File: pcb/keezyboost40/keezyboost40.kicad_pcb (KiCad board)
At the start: 2 copper layers, 217.6 x 68.1 mm, 92 parts, among them SW1 SW_SPST, SW10 SW_SPST, SW11 SW_SPST, SW12 SW_SPST, SW13 SW_SPST, SW14 SW_SPST, SW15 SW_SPST, SW16 SW_SPST, SW17 SW_SPST, SW18 SW_SPST, SW19 SW_SPST, SW2 SW_SPST, SW20 SW_SPST, SW21 SW_SPST, SW22 SW_SPST, SW23 SW_SPST, SW24 SW_SPST, SW25 SW_SPST, SW26 SW_SPST, SW27 SW_SPST, SW28 SW_SPST, SW29 SW_SPST, SW3 SW_SPST, SW30 SW_SPST, SW31 SW_SPST, SW32 SW_SPST, SW33 SW_SPST, SW34 SW_SPST, SW35 SW_SPST, SW36 SW_SPST, SW37 SW_SPST, SW38 SW_SPST, SW39 SW_SPST, SW4 SW_SPST, SW40 SW_SPST, SW5 SW_SPST, SW6 SW_SPST, SW7 SW_SPST, SW8 SW_SPST, SW9 SW_SPST, U1 Pico, U2 ST7735_1.8inch

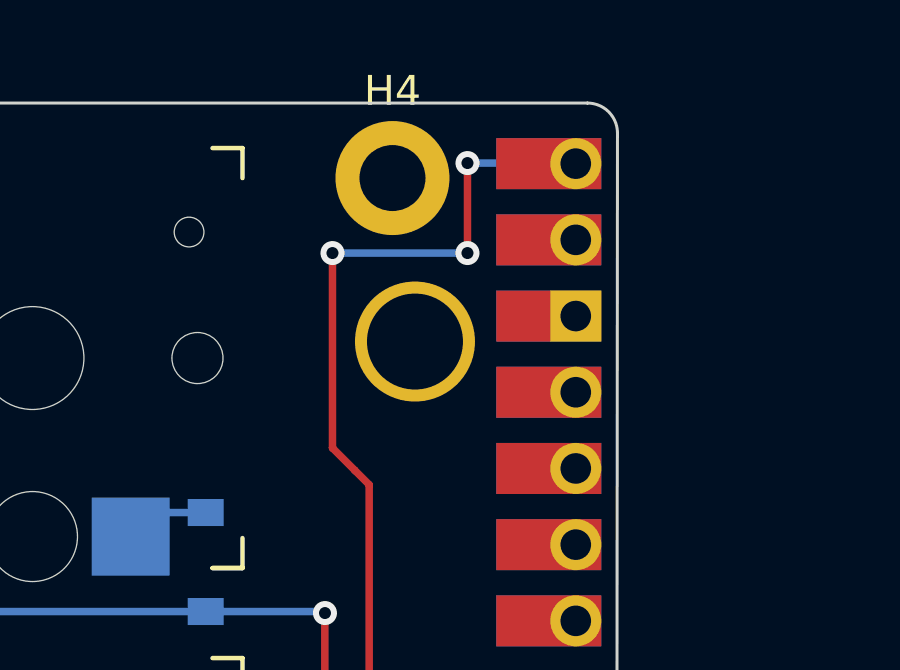
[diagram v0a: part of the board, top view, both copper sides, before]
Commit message: make lcd use 3.3v over 5v
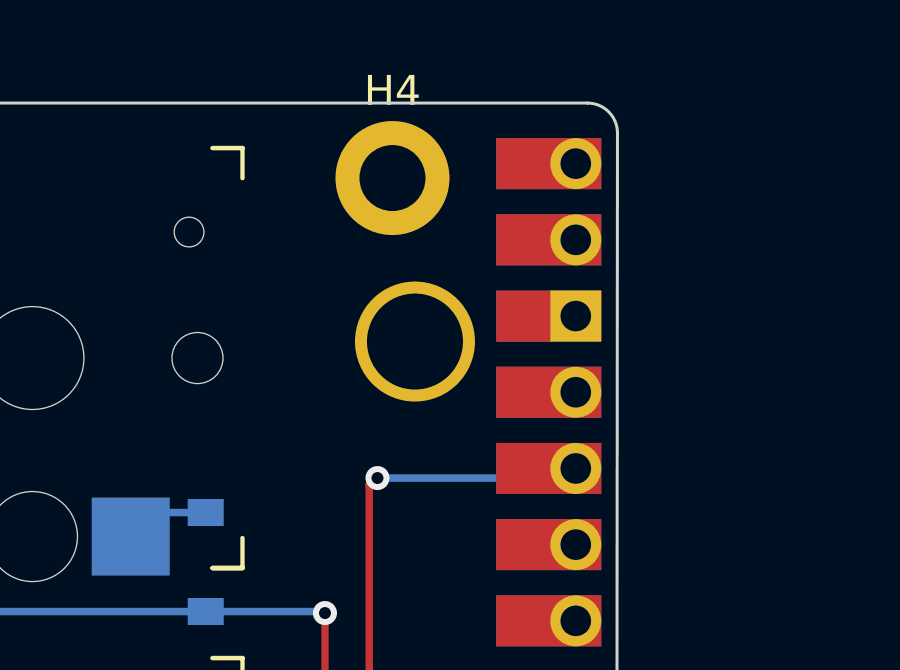
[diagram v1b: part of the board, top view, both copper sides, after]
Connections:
- U1 pad 36: unconnected-(U1-Pad36) -> vcc
- U1 pad 40: vcc -> unconnected-(U1-Pad40)
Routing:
- net vcc: track 73.1 -> 60.8 mm, vias 5 -> 3
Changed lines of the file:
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@@
   (net 68 "sck")
   (net 69 "sda")
-  (net 70 "unconnected-(U1-Pad36)")
+  (net 70 "unconnected-(U1-Pad40)")
   (net 71 "unconnected-(U1-Pad28)")
   (net 72 "unconnected-(U1-Pad30)")
@@
       (net 75 "unconnected-(U1-Pad35)") (pinfunction "ADC_VREF") (pintype "power_in+no_connect"))
     (pad "36" smd rect locked (at 8.89 13.97) (size 3.5 1.7) (drill (offset -0.9 0)) (layers "F.Cu" "F.Mask")
-      (net 70 "unconnected-(U1-Pad36)") (pinfunction "3V3") (pintype "power_in+no_connect"))
+      (net 78 "vcc") (pinfunction "3V3") (pintype "power_in"))
     (pad "36" thru_hole oval locked (at 8.89 13.97 180) (size 1.7 1.7) (drill 1.02) (layers *.Cu *.Mask)
-      (net 70 "unconnected-(U1-Pad36)") (pinfunction "3V3") (pintype "power_in+no_connect"))
+      (net 78 "vcc") (pinfunction "3V3") (pintype "power_in"))
     (pad "36" smd rect locked (at 8.89 13.97 180) (size 3.5 1.7) (drill (offset 0.9 0)) (layers "B.Cu" "B.Mask")
-      (net 70 "unconnected-(U1-Pad36)") (pinfunction "3V3") (pintype "power_in+no_connect"))
+      (net 78 "vcc") (pinfunction "3V3") (pintype "power_in"))
     (pad "37" smd rect locked (at 8.89 16.51) (size 3.5 1.7) (drill (offset -0.9 0)) (layers "F.Cu" "F.Mask")
       (net 76 "unconnected-(U1-Pad37)") (pinfunction "3V3_EN") (pintype "input+no_connect"))
@@
       (net 77 "unconnected-(U1-Pad39)") (pinfunction "VSYS") (pintype "power_in+no_connect"))
     (pad "40" smd rect locked (at 8.89 24.13 180) (size 3.5 1.7) (drill (offset 0.9 0)) (layers "B.Cu" "B.Mask")
-      (net 78 "vcc") (pinfunction "VBUS") (pintype "power_in"))
+      (net 70 "unconnected-(U1-Pad40)") (pinfunction "VBUS") (pintype "power_in+no_connect"))
     (pad "40" thru_hole oval locked (at 8.89 24.13 180) (size 1.7 1.7) (drill 1.02) (layers *.Cu *.Mask)
-      (net 78 "vcc") (pinfunction "VBUS") (pintype "power_in"))
+      (net 70 "unconnected-(U1-Pad40)") (pinfunction "VBUS") (pintype "power_in+no_connect"))
     (pad "40" smd rect locked (at 8.89 24.13) (size 3.5 1.7) (drill (offset -0.9 0)) (layers "F.Cu" "F.Mask")
-      (net 78 "vcc") (pinfunction "VBUS") (pintype "power_in"))
+      (net 70 "unconnected-(U1-Pad40)") (pinfunction "VBUS") (pintype "power_in+no_connect"))
     (group "" (id 2eefb77a-c30b-42f2-a0dd-3b92e0293566)
       (members
@@
   (segment (start 101.862256 75.775489) (end 124.724511 75.775489) (width 0.25) (layer "B.Cu") (net 69))
   (segment (start 101.488084 76.149661) (end 101.862256 75.775489) (width 0.25) (layer "B.Cu") (net 69))
+  (segment (start 112.09 14.5) (end 112.11 14.52) (width 0.25) (layer "B.Cu") (net 70))
+  (segment (start 105.224511 25.224511) (end 105.449022 25) (width 0.25) (layer "F.Cu") (net 78))
   (segment (start 105.224511 68.322562) (end 105.5 68.598051) (width 0.25) (layer "F.Cu") (net 78))
   (segment (start 111 68.75) (end 111 71.84) (width 0.25) (layer "F.Cu") (net 78))
   (segment (start 111 71.84) (end 112.11 72.95) (width 0.25) (layer "F.Cu") (net 78))
   (segment (start 105.224511 25.224511) (end 105.224511 68.322562) (width 0.25) (layer "F.Cu") (net 78))
-  (segment (start 104.75 24.75) (end 104 24) (width 0.25) (layer "F.Cu") (net 78))
-  (segment (start 108.5 17.5) (end 108.5 14.5) (width 0.25) (layer "F.Cu") (net 78))
-  (segment (start 104.75 24.75) (end 105.224511 25.224511) (width 0.25) (layer "F.Cu") (net 78))
-  (segment (start 104 24) (end 104 17.5) (width 0.25) (layer "F.Cu") (net 78))
-  (via (at 104 17.5) (size 0.8) (drill 0.4) (layers "F.Cu" "B.Cu") (net 78))
-  (via (at 108.5 14.5) (size 0.8) (drill 0.4) (layers "F.Cu" "B.Cu") (net 78))
-  (via (at 108.5 17.5) (size 0.8) (drill 0.4) (layers "F.Cu" "B.Cu") (net 78))
+  (segment (start 105.449022 25) (end 105.5 25) (width 0.25) (layer "F.Cu") (net 78))
+  (via (at 105.5 25) (size 0.8) (drill 0.4) (layers "F.Cu" "B.Cu") (net 78))
   (via (at 111 68.75) (size 0.8) (drill 0.4) (layers "F.Cu" "B.Cu") (net 78))
   (via (at 105.5 68.598051) (size 0.8) (drill 0.4) (layers "F.Cu" "B.Cu") (net 78))
   (segment (start 110.848051 68.598051) (end 111 68.75) (width 0.25) (layer "B.Cu") (net 78))
-  (segment (start 108.5 14.5) (end 112.09 14.5) (width 0.25) (layer "B.Cu") (net 78))
-  (segment (start 104 17.5) (end 108.5 17.5) (width 0.25) (layer "B.Cu") (net 78))
+  (segment (start 105.5 25) (end 111.79 25) (width 0.25) (layer "B.Cu") (net 78))
+  (segment (start 111.79 25) (end 112.11 24.68) (width 0.25) (layer "B.Cu") (net 78))
   (segment (start 105.5 68.598051) (end 110.848051 68.598051) (width 0.25) (layer "B.Cu") (net 78))
-  (segment (start 112.09 14.5) (end 112.11 14.52) (width 0.25) (layer "B.Cu") (net 78))
   (group "" (id 7b4c85be-e685-4876-acb4-59efa78bd468)
     (members

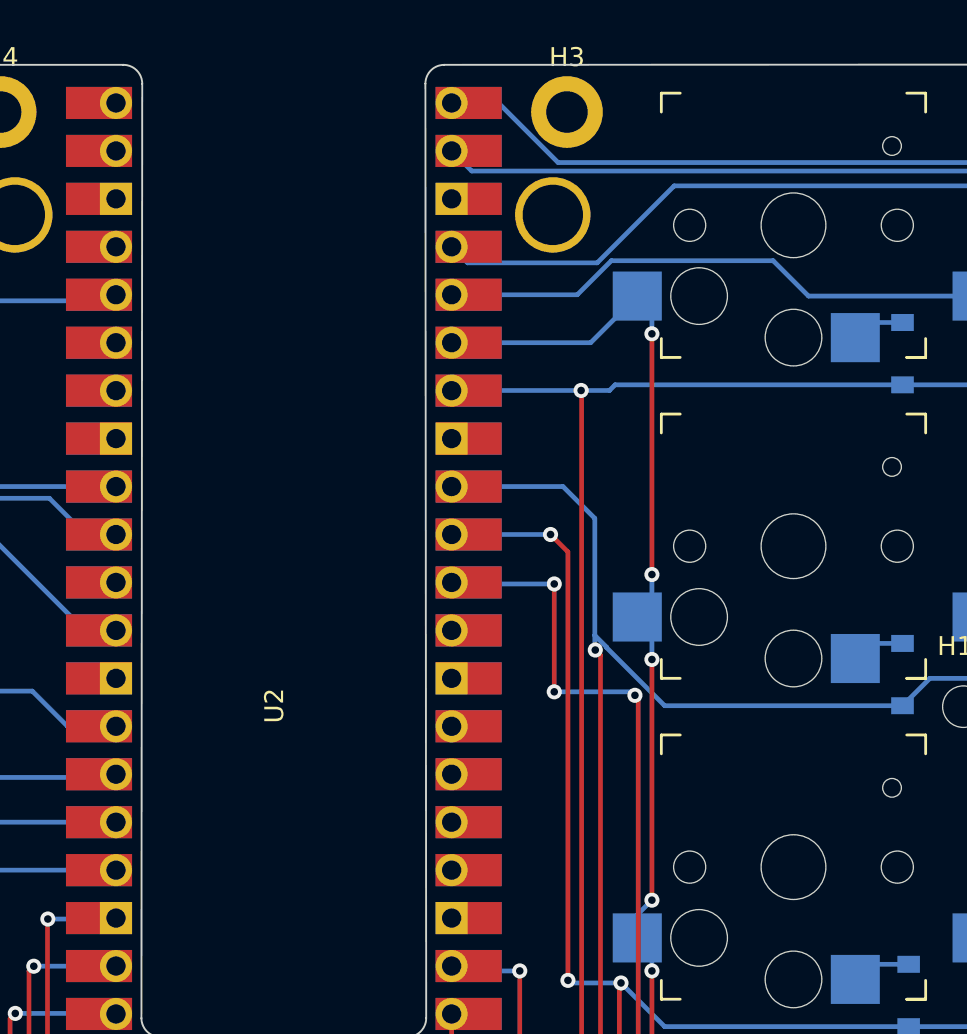
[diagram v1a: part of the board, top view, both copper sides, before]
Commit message: add reset button
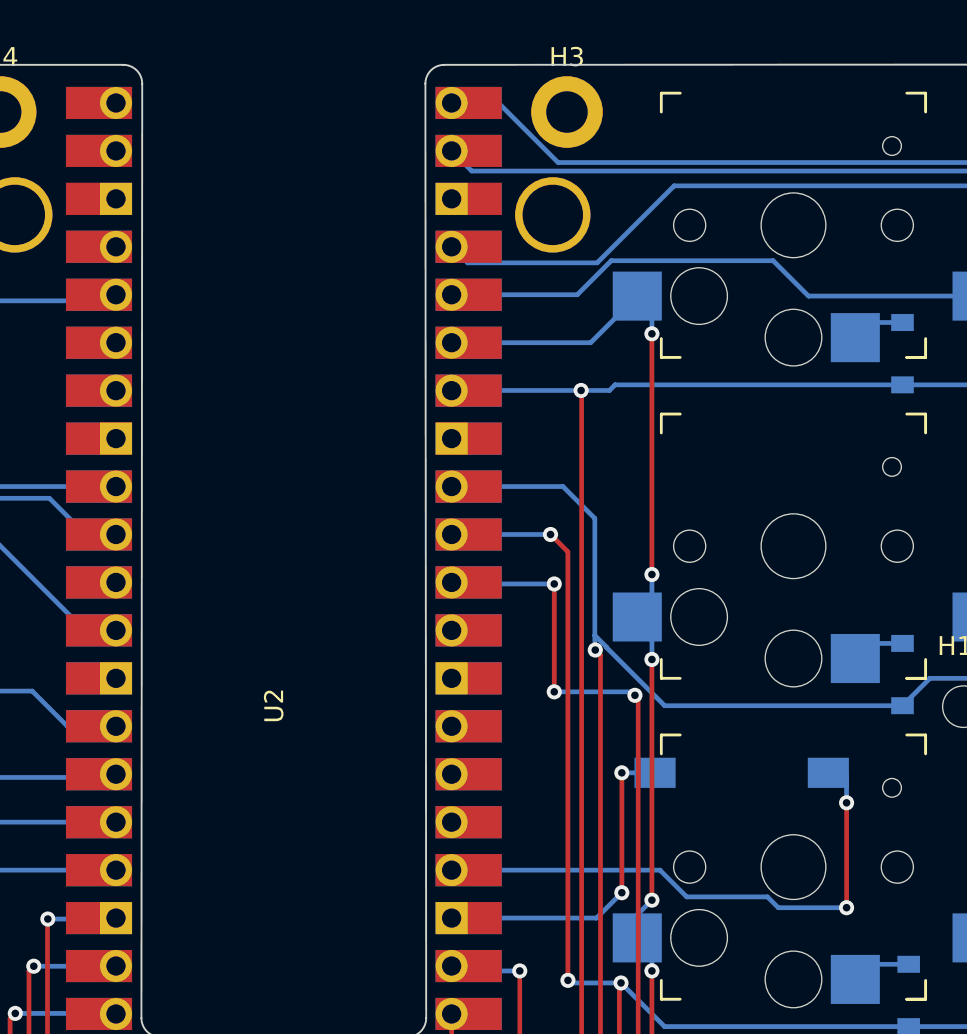
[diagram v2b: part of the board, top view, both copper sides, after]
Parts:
- added SW41: SW_SPST, Button_Switch_SMD:SW_SPST_FSMSM, B.Cu at (145.3, 50.0)
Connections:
- U1 pad 17: /buzzer -> Net-(SW41-Pad2)
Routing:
- net Net-(SW41-Pad2): track 0.00 -> 29.0 mm, vias 0 -> 2
- net gnd: track 25.0 -> 43.4 mm, vias 5 -> 7
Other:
- board text added: "i cant see the silkscreen"
- board text removed: "bro i cant see the silkscreen"
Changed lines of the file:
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@@
   (net 45 "Net-(D40-Pad2)")
   (net 46 "lcd_reset")
-  (net 47 "/buzzer")
+  (net 47 "Net-(SW41-Pad2)")
   (net 48 "c1")
   (net 49 "c2")
@@
       (net 64 "unconnected-(U1-Pad16)") (pinfunction "GPIO12") (pintype "bidirectional+no_connect"))
     (pad "17" smd rect locked (at -8.89 -16.51) (size 3.5 1.7) (drill (offset 0.9 0)) (layers "F.Cu" "F.Mask")
-      (net 47 "/buzzer") (pinfunction "GPIO13") (pintype "bidirectional"))
+      (net 47 "Net-(SW41-Pad2)") (pinfunction "GPIO13") (pintype "bidirectional"))
     (pad "17" thru_hole oval locked (at -8.89 -16.51 180) (size 1.7 1.7) (drill 1.02) (layers *.Cu *.Mask)
-      (net 47 "/buzzer") (pinfunction "GPIO13") (pintype "bidirectional"))
+      (net 47 "Net-(SW41-Pad2)") (pinfunction "GPIO13") (pintype "bidirectional"))
     (pad "17" smd rect locked (at -8.89 -16.51 180) (size 3.5 1.7) (drill (offset -0.9 0)) (layers "B.Cu" "B.Mask")
-      (net 47 "/buzzer") (pinfunction "GPIO13") (pintype "bidirectional"))
+      (net 47 "Net-(SW41-Pad2)") (pinfunction "GPIO13") (pintype "bidirectional"))
     (pad "18" smd rect locked (at -8.89 -19.05 180) (size 3.5 1.7) (drill (offset -0.9 0)) (layers "B.Cu" "B.Mask")
       (net 1 "gnd") (pinfunction "GND") (pintype "power_in"))
@@
     )
   )
+  (footprint "Button_Switch_SMD:SW_SPST_FSMSM" (layer "B.Cu")
+    (at 145.25625 50.00625)
+    (descr "http://www.te.com/commerce/DocumentDelivery/DDEController?Action=srchrtrv&DocNm=1437566-3&DocType=Customer+Drawing&DocLang=English")
+    (tags "SPST button tactile switch")
+    (property "Sheetfile" "keezyboost40.kicad_sch")
+    (property "Sheetname" "")
+    (attr smd)
+    (fp_text reference "SW41" (at 0 2.6) (layer "B.SilkS")
+      (effects (font (size 1 1) (thickness 0.15)) (justify mirror))
+    )
+    (fp_text value "SW_SPST" (at 0 -3) (layer "B.Fab")
+      (effects (font (size 1 1) (thickness 0.15)) (justify mirror))
+    )
+    (fp_text user "${REFERENCE}" (at 0 2.6) (layer "B.Fab")
+      (effects (font (size 1 1) (thickness 0.15)) (justify mirror))
+    )
+    (fp_line (start -3.06 -1.81) (end -3.06 1.81) (layer "B.SilkS") (width 0.12))
+    (fp_line (start -3.06 1.81) (end 3.06 1.81) (layer "B.SilkS") (width 0.12))
+    (fp_line (start 3.06 1.81) (end 3.06 -1.81) (layer "B.SilkS") (width 0.12))
+    (fp_line (start 3.06 -1.81) (end -3.06 -1.81) (layer "B.SilkS") (width 0.12))
+    (fp_line (start 5.95 2) (end 5.95 -2) (layer "B.CrtYd") (width 0.05))
+    (fp_line (start -5.95 2) (end -5.95 -2) (layer "B.CrtYd") (width 0.05))
+    (fp_line (start -5.95 -2) (end 5.95 -2) (layer "B.CrtYd") (width 0.05))
+    (fp_line (start -5.95 2) (end 5.95 2) (layer "B.CrtYd") (width 0.05))
+    (fp_line (start -3 -1.75) (end 3 -1.75) (layer "B.Fab") (width 0.1))
+    (fp_line (start -1.5 0.8) (end -1.5 -0.8) (layer "B.Fab") (width 0.1))
+    (fp_line (start -3 1.75) (end -3 -1.75) (layer "B.Fab") (width 0.1))
+    (fp_line (start 3 1.75) (end 3 -1.75) (layer "B.Fab") (width 0.1))
+    (fp_line (start 1.5 0.8) (end 1.5 -0.8) (layer "B.Fab") (width 0.1))
+    (fp_line (start -1.5 0.8) (end 1.5 0.8) (layer "B.Fab") (width 0.1))
+    (fp_line (start -1.75 -1) (end -1.75 1) (layer "B.Fab") (width 0.1))
+    (fp_line (start -1.75 1) (end 1.75 1) (layer "B.Fab") (width 0.1))
+    (fp_line (start 1.75 -1) (end -1.75 -1) (layer "B.Fab") (width 0.1))
+    (fp_line (start -3 1.75) (end 3 1.75) (layer "B.Fab") (width 0.1))
+    (fp_line (start -1.5 -0.8) (end 1.5 -0.8) (layer "B.Fab") (width 0.1))
+    (fp_line (start 1.75 1) (end 1.75 -1) (layer "B.Fab") (width 0.1))
+    (pad "1" smd rect (at -4.59 0) (size 2.18 1.6) (layers "B.Cu" "B.Paste" "B.Mask")
+      (net 1 "gnd") (pinfunction "A") (pintype "passive"))
+    (pad "2" smd rect (at 4.59 0) (size 2.18 1.6) (layers "B.Cu" "B.Paste" "B.Mask")
+      (net 47 "Net-(SW41-Pad2)") (pinfunction "B") (pintype "passive"))
+    (model "${KICAD6_3DMODEL_DIR}/Button_Switch_SMD.3dshapes/SW_SPST_FSMSM.wrl"
+      (offset (xyz 0 0 0))
+      (scale (xyz 1 1 1))
+      (rotate (xyz 0 0 0))
+    )
+  )
   (footprint "Diode_SMD:D_SOD-123" locked (layer "B.Cu")
     (at 171.7751 27.8 90)
@@
     (effects (font (size 1 1) (thickness 0.15)) (justify mirror))
   )
-  (gr_text "bro i cant\nsee the\nsilkscreen" (at 58 46.2) (layer "B.SilkS")
+  (gr_text "i cant\nsee the\nsilkscreen" (at 58 46.2) (layer "B.SilkS")
     (effects (font (size 10 10) (thickness 1.25)) (justify mirror))
   )
   (segment (start 114.55 71) (end 114.5 71) (width 0.25) (layer "F.Cu") (net 1))
+  (segment (start 138.90625 56.35625) (end 138.90625 50.00625) (width 0.25) (layer "F.Cu") (net 1))
   (segment (start 114.65 71.1) (end 114.55 71) (width 0.25) (layer "F.Cu") (net 1))
   (segment (start 114.65 72.95) (end 114.65 71.1) (width 0.25) (layer "F.Cu") (net 1))
@@
   (via (at 111.75 71) (size 0.8) (drill 0.4) (layers "F.Cu" "B.Cu") (net 1))
   (via (at 111.75 64.229502) (size 0.8) (drill 0.4) (layers "F.Cu" "B.Cu") (net 1))
+  (via (at 138.90625 50.00625) (size 0.8) (drill 0.4) (layers "F.Cu" "B.Cu") (net 1))
   (via (at 114.5 71) (size 0.8) (drill 0.4) (layers "F.Cu" "B.Cu") (net 1))
   (via (at 108.479502 64.229502) (size 0.8) (drill 0.4) (layers "F.Cu" "B.Cu") (net 1))
+  (via (at 138.90625 56.35625) (size 0.8) (drill 0.4) (layers "F.Cu" "B.Cu") (net 1))
   (via (at 108.5 57.75) (size 0.8) (drill 0.4) (layers "F.Cu" "B.Cu") (net 1))
+  (segment (start 138.90625 50.00625) (end 141.46 50.00625) (width 0.25) (layer "B.Cu") (net 1))
+  (segment (start 129.89 57.7) (end 137.5625 57.7) (width 0.25) (layer "B.Cu") (net 1))
   (segment (start 111.75 64.229502) (end 108.479502 64.229502) (width 0.25) (layer "B.Cu") (net 1))
   (segment (start 114.5 71) (end 111.75 71) (width 0.25) (layer "B.Cu") (net 1))
   (segment (start 112.06 57.75) (end 112.11 57.7) (width 0.25) (layer "B.Cu") (net 1))
+  (segment (start 137.5625 57.7) (end 138.90625 56.35625) (width 0.25) (layer "B.Cu") (net 1))
   (segment (start 108.5 57.75) (end 112.06 57.75) (width 0.25) (layer "B.Cu") (net 1))
   (segment (start 103.75 65.5) (end 104.5 66.25) (width 0.25) (layer "F.Cu") (net 2))
@@
   (segment (start 129.89 60.24) (end 130.15 60.5) (width 0.25) (layer "B.Cu") (net 46))
   (segment (start 130.15 60.5) (end 133.5 60.5) (width 0.25) (layer "B.Cu") (net 46))
+  (segment (start 150.8125 57.15) (end 150.8125 51.59375) (width 0.25) (layer "F.Cu") (net 47))
+  (via (at 150.8125 51.59375) (size 0.8) (drill 0.4) (layers "F.Cu" "B.Cu") (net 47))
+  (via (at 150.8125 57.15) (size 0.8) (drill 0.4) (layers "F.Cu" "B.Cu") (net 47))
+  (segment (start 150.8125 50.17875) (end 150.64 50.00625) (width 0.25) (layer "B.Cu") (net 47))
+  (segment (start 146.622839 56.577162) (end 147.195677 57.15) (width 0.25) (layer "B.Cu") (net 47))
+  (segment (start 140.926992 55.16) (end 142.344154 56.577162) (width 0.25) (layer "B.Cu") (net 47))
+  (segment (start 147.195677 57.15) (end 150.8125 57.15) (width 0.25) (layer "B.Cu") (net 47))
+  (segment (start 142.344154 56.577162) (end 146.622839 56.577162) (width 0.25) (layer "B.Cu") (net 47))
+  (segment (start 129.89 55.16) (end 140.926992 55.16) (width 0.25) (layer "B.Cu") (net 47))
+  (segment (start 150.8125 51.59375) (end 150.8125 50.17875) (width 0.25) (layer "B.Cu") (net 47))
   (segment (start 13.725 58.75) (end 13.725 75.75) (width 0.25) (layer "B.Cu") (net 48))
   (segment (start 13.725 41.75) (end 13.725 58.75) (width 0.25) (layer "B.Cu") (net 48))
@@
   (segment (start 101.862256 75.775489) (end 124.724511 75.775489) (width 0.25) (layer "B.Cu") (net 69))
   (segment (start 101.488084 76.149661) (end 101.862256 75.775489) (width 0.25) (layer "B.Cu") (net 69))
-  (segment (start 112.09 14.5) (end 112.11 14.52) (width 0.25) (layer "B.Cu") (net 70))
   (segment (start 105.224511 25.224511) (end 105.449022 25) (width 0.25) (layer "F.Cu") (net 78))
   (segment (start 105.224511 68.322562) (end 105.5 68.598051) (width 0.25) (layer "F.Cu") (net 78))
